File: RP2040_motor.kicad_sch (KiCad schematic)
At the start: 0 parts

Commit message: WORK IN PROGRESS updates from design review - clean schematic and PCB
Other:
- note added: "60 Volt input maximum 100 Amp peak current draw 50 Amp peak per motor absolute maximum"
- note added: "ADDITIONAL GPIO"
- note added: "CAN"
- note added: "CAN/ESTOP IN"
- note added: "CAN/ESTOP OUT"
- note added: "CLICK BELOW FOR CPUs AND I/O LAYOUT"
- note added: "CLICK BELOW FOR GATE DRIVE AND MOTOR CONNECTIONS"
- note added: "CPU1"
- note added: "CPU2"
- note added: "CURRENT SENSE"
- note added: "ENCODER1"
- note added: "ENCODER2"
- note added: "GATE DRIVE"
- note added: "GPIO"
- note added: "MOTOR1"
- note added: "MOTOR2"
- note added: "Serial"
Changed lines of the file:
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@@
     (comment 2 "LICENSE: CERN-OHL-P")
   )
-  (sheet (at 67.31 37.465) (size 109.855 65.405) (fields_autoplaced)
+  (arc (start 306.705 142.875) (mid 307.0996 143.8275) (end 306.705 144.78)
+    (stroke (width 0) (type default))
+    (fill (type none))
+  )
+  (arc (start 308.61 108.585) (mid 305.7525 109.7686) (end 302.895 108.585)
+    (stroke (width 0) (type default))
+    (fill (type none))
+  )
+  (arc (start 329.565 100.33) (mid 334.88 112.2635) (end 330.2 124.46)
+    (stroke (width 0) (type default))
+    (fill (type none))
+  )
+  (arc (start 248.92 102.235) (mid 247.65 102.761) (end 246.38 102.235)
+    (stroke (width 0) (type default))
+    (fill (type none))
+  )
+  (arc (start 329.565 109.855) (mid 332.3812 115.756) (end 330.2 121.92)
+    (stroke (width 0) (type default))
+    (fill (type none))
+  )
+  (arc (start 284.48 106.045) (mid 279.7175 108.0177) (end 274.955 106.045)
+    (stroke (width 0) (type default))
+    (fill (type none))
+  )
+  (arc (start 284.48 101.6) (mid 279.586 103.2552) (end 274.955 100.965)
+    (stroke (width 0) (type default))
+    (fill (type none))
+  )
+  (arc (start 248.92 112.395) (mid 247.65 112.921) (end 246.38 112.395)
+    (stroke (width 0) (type default))
+    (fill (type none))
+  )
+  (arc (start 257.81 153.035) (mid 258.4675 154.6225) (end 257.81 156.21)
+    (stroke (width 0) (type default))
+    (fill (type none))
+  )
+  (arc (start 277.495 140.97) (mid 276.225 141.496) (end 274.955 140.97)
+    (stroke (width 0) (type default))
+    (fill (type none))
+  )
+  (arc (start 253.365 128.27) (mid 252.3129 125.73) (end 253.365 123.19)
+    (stroke (width 0) (type default))
+    (fill (type none))
+  )
+  (arc (start 266.065 128.27) (mid 265.0129 125.73) (end 266.065 123.19)
+    (stroke (width 0) (type default))
+    (fill (type none))
+  )
+  (rectangle (start 308.61 95.885) (end 329.565 104.775)
+    (stroke (width 0) (type default))
+    (fill (type color) (color 255 255 194 1))
+  )
+  (arc (start 277.495 139.065) (mid 276.225 139.591) (end 274.955 139.065)
+    (stroke (width 0) (type default))
+    (fill (type none))
+  )
+  (rectangle (start 220.98 109.22) (end 246.38 118.11)
+    (stroke (width 0) (type default))
+    (fill (type color) (color 255 255 194 1))
+  )
+  (arc (start 285.115 118.745) (mid 279.9035 120.5317) (end 274.955 118.11)
+    (stroke (width 0) (type default))
+    (fill (type none))
+  )
+  (rectangle (start 284.48 95.885) (end 302.895 111.76)
+    (stroke (width 0) (type default))
+    (fill (type color) (color 255 255 194 1))
+  )
+  (arc (start 299.72 141.605) (mid 297.815 142.3941) (end 295.91 141.605)
+    (stroke (width 0) (type default))
+    (fill (type none))
+  )
+  (rectangle (start 285.115 117.475) (end 330.2 126.365)
+    (stroke (width 0) (type default))
+    (fill (type color) (color 255 255 194 1))
+  )
+  (arc (start 267.335 128.27) (mid 266.2829 125.73) (end 267.335 123.19)
+    (stroke (width 0) (type default))
+    (fill (type none))
+  )
+  (rectangle (start 308.61 105.41) (end 329.565 114.3)
+    (stroke (width 0) (type default))
+    (fill (type color) (color 255 255 194 1))
+  )
+  (arc (start 284.48 104.14) (mid 279.7175 106.1127) (end 274.955 104.14)
+    (stroke (width 0) (type default))
+    (fill (type none))
+  )
+  (rectangle (start 220.98 99.06) (end 246.38 107.95)
+    (stroke (width 0) (type default))
+    (fill (type color) (color 255 255 194 1))
+  )
+  (rectangle (start 299.72 130.175) (end 329.565 142.875)
+    (stroke (width 0) (type default))
+    (fill (type color) (color 255 255 194 1))
+  )
+  (arc (start 255.27 128.27) (mid 254.2179 125.73) (end 255.27 123.19)
+    (stroke (width 0) (type default))
+    (fill (type none))
+  )
+  (arc (start 284.48 105.41) (mid 279.7175 107.3827) (end 274.955 105.41)
+    (stroke (width 0) (type default))
+    (fill (type none))
+  )
+  (arc (start 260.985 153.035) (mid 261.6425 154.6225) (end 260.985 156.21)
+    (stroke (width 0) (type default))
+    (fill (type none))
+  )
+  (rectangle (start 248.92 128.27) (end 274.955 153.035)
+    (stroke (width 0) (type default))
+    (fill (type color) (color 255 255 194 1))
+  )
+  (arc (start 255.27 153.035) (mid 255.9275 154.6225) (end 255.27 156.21)
+    (stroke (width 0) (type default))
+    (fill (type none))
+  )
+  (arc (start 285.115 120.65) (mid 280.035 122.7542) (end 274.955 120.65)
+    (stroke (width 0) (type default))
+    (fill (type none))
+  )
+  (arc (start 299.72 139.7) (mid 297.815 140.4891) (end 295.91 139.7)
+    (stroke (width 0) (type default))
+    (fill (type none))
+  )
+  (arc (start 308.61 99.695) (mid 305.7525 100.8786) (end 302.895 99.695)
+    (stroke (width 0) (type default))
+    (fill (type none))
+  )
+  (arc (start 308.61 142.875) (mid 309.0046 143.8275) (end 308.61 144.78)
+    (stroke (width 0) (type default))
+    (fill (type none))
+  )
+  (arc (start 284.48 103.505) (mid 279.586 105.1602) (end 274.955 102.87)
+    (stroke (width 0) (type default))
+    (fill (type none))
+  )
+  (rectangle (start 248.92 98.425) (end 274.955 123.19)
+    (stroke (width 0) (type default))
+    (fill (type color) (color 255 255 194 1))
+  )
+  (rectangle (start 277.495 135.89) (end 295.91 153.035)
+    (stroke (width 0) (type default))
+    (fill (type color) (color 255 255 194 1))
+  )
+  (arc (start 284.48 102.235) (mid 279.586 103.8902) (end 274.955 101.6)
+    (stroke (width 0) (type default))
+    (fill (type none))
+  )
+  (rectangle (start 248.92 156.21) (end 276.225 170.815)
+    (stroke (width 0) (type default))
+    (fill (type color) (color 255 255 194 1))
+  )
+  (rectangle (start 299.72 144.78) (end 329.565 157.48)
+    (stroke (width 0) (type default))
+    (fill (type color) (color 255 255 194 1))
+  )
+  (text "CURRENT SENSE" (at 288.925 123.825 0)
+    (effects (font (size 3 3)) (justify left bottom))
+  )
+  (text "CAN/ESTOP\nOUT" (at 301.625 154.94 0)
+    (effects (font (size 3 3)) (justify left bottom))
+  )
+  (text "MOTOR1" (at 309.88 102.235 0)
+    (effects (font (size 3 3)) (justify left bottom))
+  )
+  (text "CAN" (at 278.765 140.97 0)
+    (effects (font (size 3 3)) (justify left bottom))
+  )
+  (text "ADDITIONAL\nGPIO" (at 250.19 167.64 0)
+    (effects (font (size 3 3)) (justify left bottom))
+  )
+  (text "GPIO" (at 267.335 126.365 0)
+    (effects (font (size 1.27 1.27)) (justify left bottom))
+  )
+  (text "CAN/ESTOP\nIN" (at 301.625 140.335 0)
+    (effects (font (size 3 3)) (justify left bottom))
+  )
+  (text "ENCODER1" (at 222.25 105.41 0)
+    (effects (font (size 3 3)) (justify left bottom))
+  )
+  (text "60 Volt input maximum\n100 Amp peak current draw\n50 Amp peak per motor absolute maximum"
+    (at 224.155 87.63 0)
+    (effects (font (size 3 3)) (justify left bottom))
+  )
+  (text "Serial" (at 245.745 126.365 0)
+    (effects (font (size 1.27 1.27)) (justify left bottom))
+  )
+  (text "CLICK BELOW FOR CPUs AND I/O LAYOUT" (at 64.135 42.545 0)
+    (effects (font (size 3 3)) (justify left bottom))
+  )
+  (text "CPU2" (at 249.555 133.35 0)
+    (effects (font (size 3 3)) (justify left bottom))
+  )
+  (text "CPU1" (at 249.555 103.505 0)
+    (effects (font (size 3 3)) (justify left bottom))
+  )
+  (text "ENCODER2" (at 222.25 115.57 0)
+    (effects (font (size 3 3)) (justify left bottom))
+  )
+  (text "MOTOR2" (at 309.88 111.76 0)
+    (effects (font (size 3 3)) (justify left bottom))
+  )
+  (text "CLICK BELOW FOR GATE DRIVE AND MOTOR CONNECTIONS" (at 57.15 130.175 0)
+    (effects (font (size 3 3)) (justify left bottom))
+  )
+  (text "GATE\nDRIVE" (at 287.655 107.95 0)
+    (effects (font (size 3 3)) (justify left bottom))
+  )
+  (sheet (at 57.15 48.26) (size 131.445 65.405) (fields_autoplaced)
     (stroke (width 0.1524) (type solid))
     (fill (color 0 0 0 0.0000))
-    (property "Sheetname" "power_and_cpu" (at 67.31 36.7534 0)
+    (property "Sheetname" "power_and_cpu" (at 57.15 47.5484 0)
       (effects (font (size 1.27 1.27)) (justify left bottom))
     )
-    (property "Sheetfile" "power_and_cpu.kicad_sch" (at 67.31 103.4546 0)
+    (property "Sheetfile" "power_and_cpu.kicad_sch" (at 57.15 114.2496 0)
       (effects (font (size 1.27 1.27)) (justify left top))
     )
@@
     )
   )
-  (sheet (at 69.215 142.24) (size 113.03 80.645) (fields_autoplaced)
+  (sheet (at 56.515 137.16) (size 131.445 80.645) (fields_autoplaced)
     (stroke (width 0.1524) (type solid))
     (fill (color 0 0 0 0.0000))
-    (property "Sheetname" "gate_drive" (at 69.215 141.5284 0)
+    (property "Sheetname" "gate_drive" (at 56.515 136.4484 0)
       (effects (font (size 1.27 1.27)) (justify left bottom))
     )
-    (property "Sheetfile" "gate_drive.kicad_sch" (at 69.215 223.4696 0)
+    (property "Sheetfile" "gate_drive.kicad_sch" (at 56.515 218.3896 0)
       (effects (font (size 1.27 1.27)) (justify left top))
     )

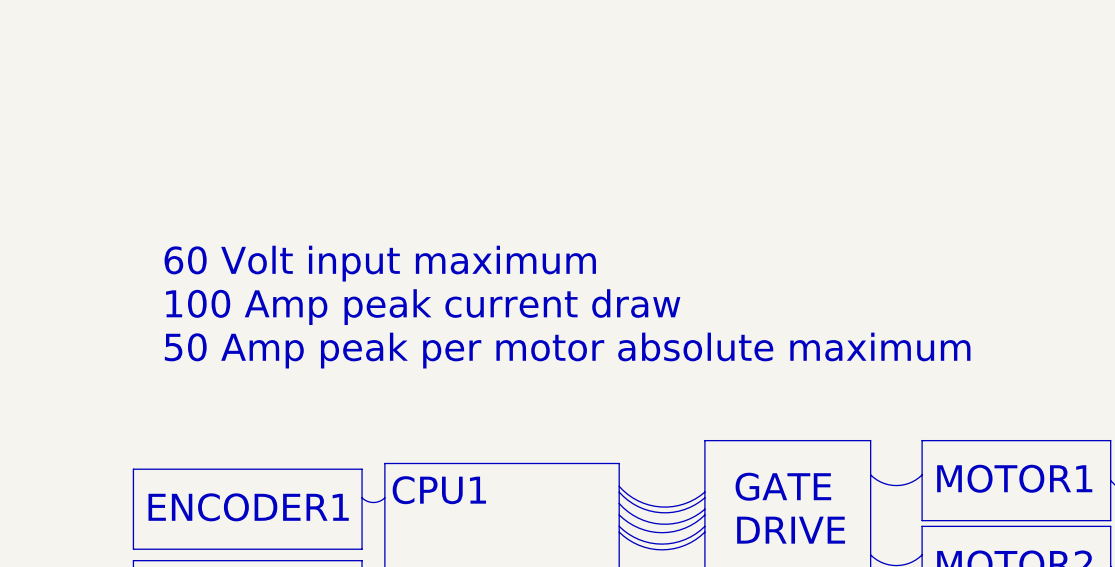
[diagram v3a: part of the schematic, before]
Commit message: Updated schematic based on many suggestions in design review. Incomplete.
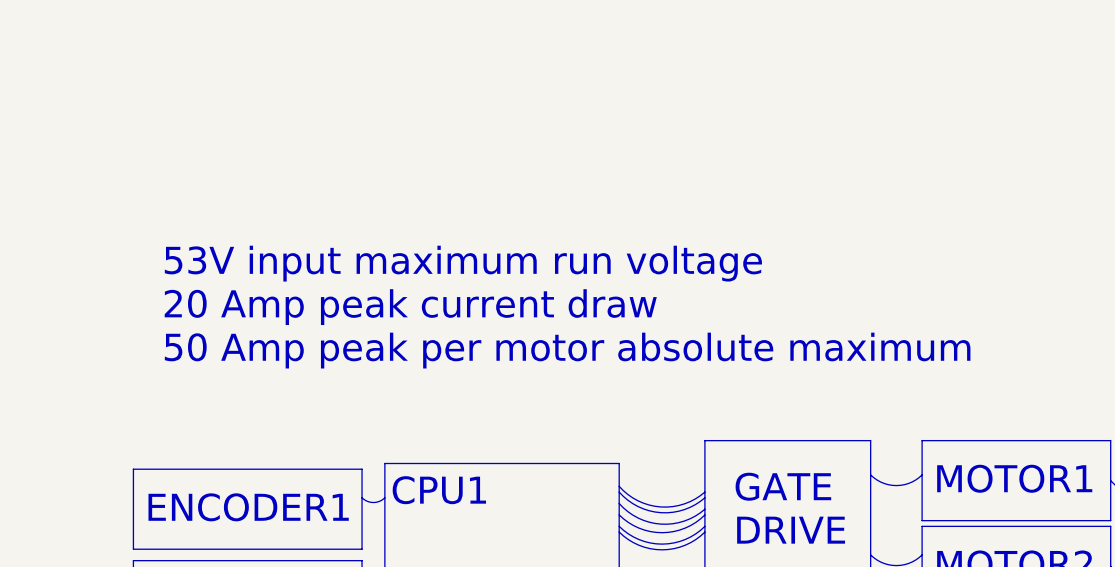
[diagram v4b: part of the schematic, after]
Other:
- note added: "53V input maximum run voltage 20 Amp peak current draw 50 Amp peak per motor absolute maximum"
- note removed: "60 Volt input maximum 100 Amp peak current draw 50 Amp peak per motor absolute maximum"
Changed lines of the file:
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@@
     (effects (font (size 3 3)) (justify left bottom))
   )
-  (text "60 Volt input maximum\n100 Amp peak current draw\n50 Amp peak per motor absolute maximum"
+  (text "53V input maximum run voltage\n20 Amp peak current draw\n50 Amp peak per motor absolute maximum"
     (at 224.155 87.63 0)
     (effects (font (size 3 3)) (justify left bottom))
